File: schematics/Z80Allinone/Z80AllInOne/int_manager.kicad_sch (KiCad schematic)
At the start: 8 parts, among them U25 74LS32, U26 74LS148, U28 74LS373

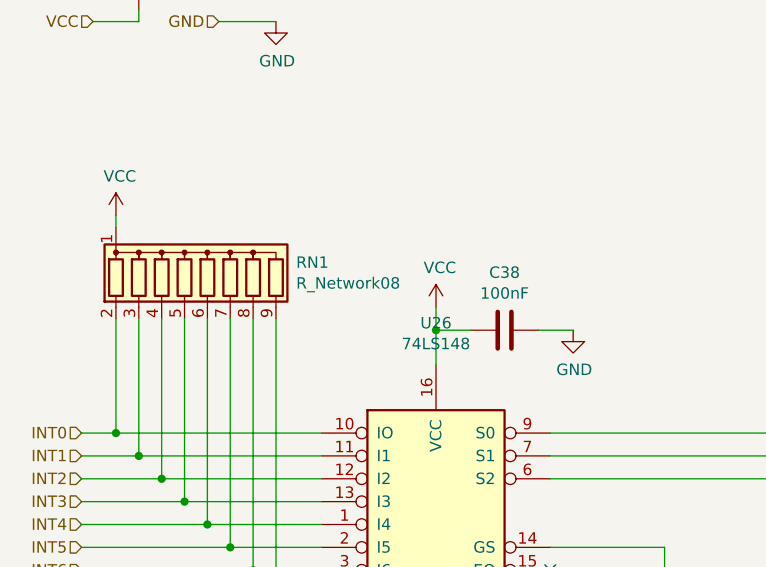
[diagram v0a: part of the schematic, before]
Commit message: Latest changes for adapt source to support Z80AllInOne adding some macros and latest schematic improvements
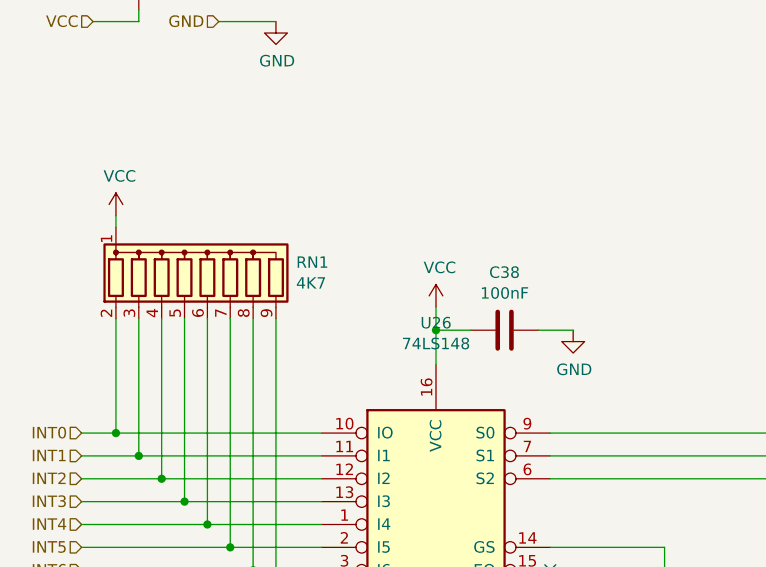
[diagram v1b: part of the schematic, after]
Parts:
- RN1: value R_Network08 -> 4K7
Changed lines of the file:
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@@
       (effects (font (size 1.27 1.27)) (justify left))
     )
-    (property "Value" "R_Network08" (id 1) (at 96.2152 59.563 0)
+    (property "Value" "4K7" (id 1) (at 96.2152 59.563 0)
       (effects (font (size 1.27 1.27)) (justify left))
     )

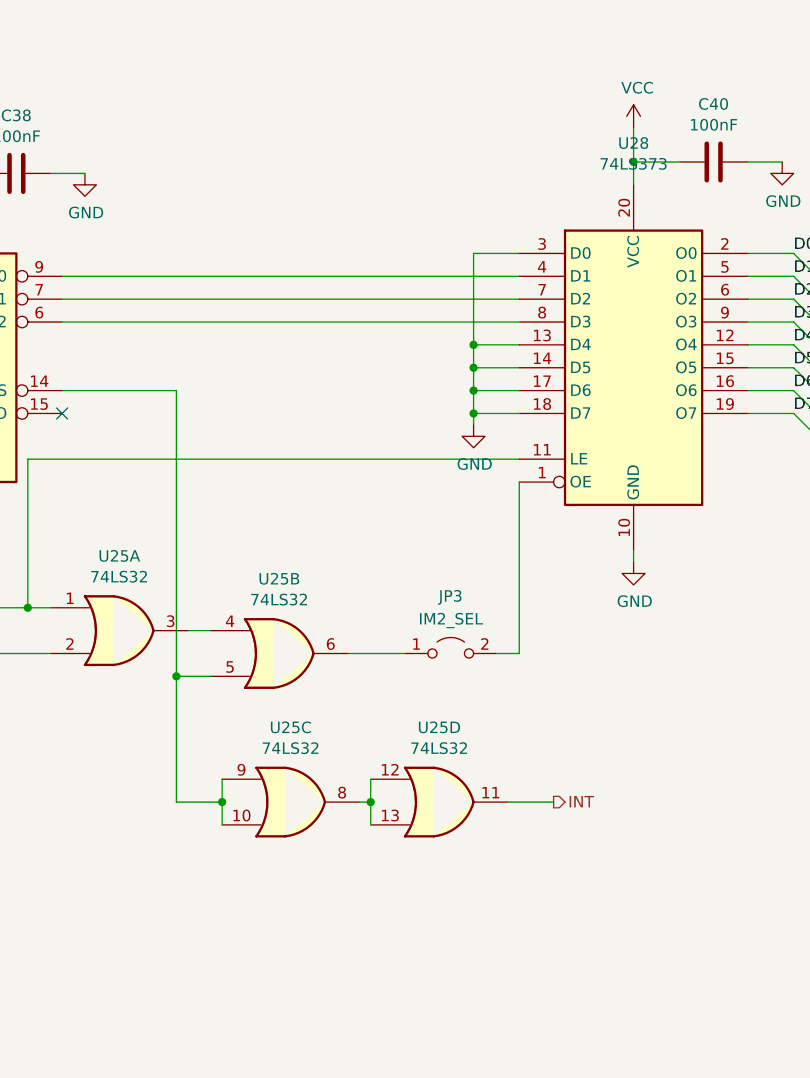
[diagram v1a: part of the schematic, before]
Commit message: Added IM 2 based routines software support
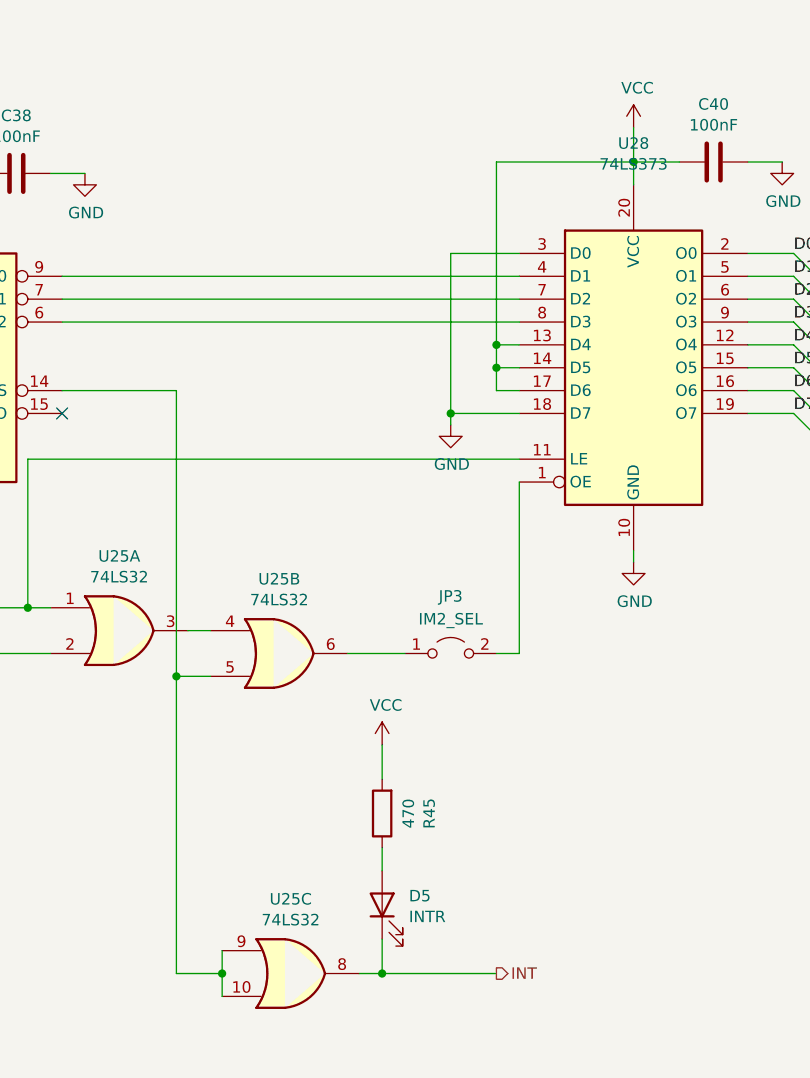
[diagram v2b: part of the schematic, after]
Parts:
- removed unit 4 of U25
- added D5: INTR, LED_THT:LED_D3.0mm, symbol Device:LED
- added R45: 470, Resistor_THT:R_Axial_DIN0207_L6.3mm_D2.5mm_P10.16mm_Horizontal, symbol Device:R
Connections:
- net GND: no longer U28.13 (D4), U28.14 (D5), U28.17 (D6)
- net INT: now also U25.8, D5.1 (K)
- net VCC: now also U28.13 (D4), U28.14 (D5), U28.17 (D6), R45.2
- new net: D5.2 (A), R45.1
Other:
- moved on the sheet: U25C

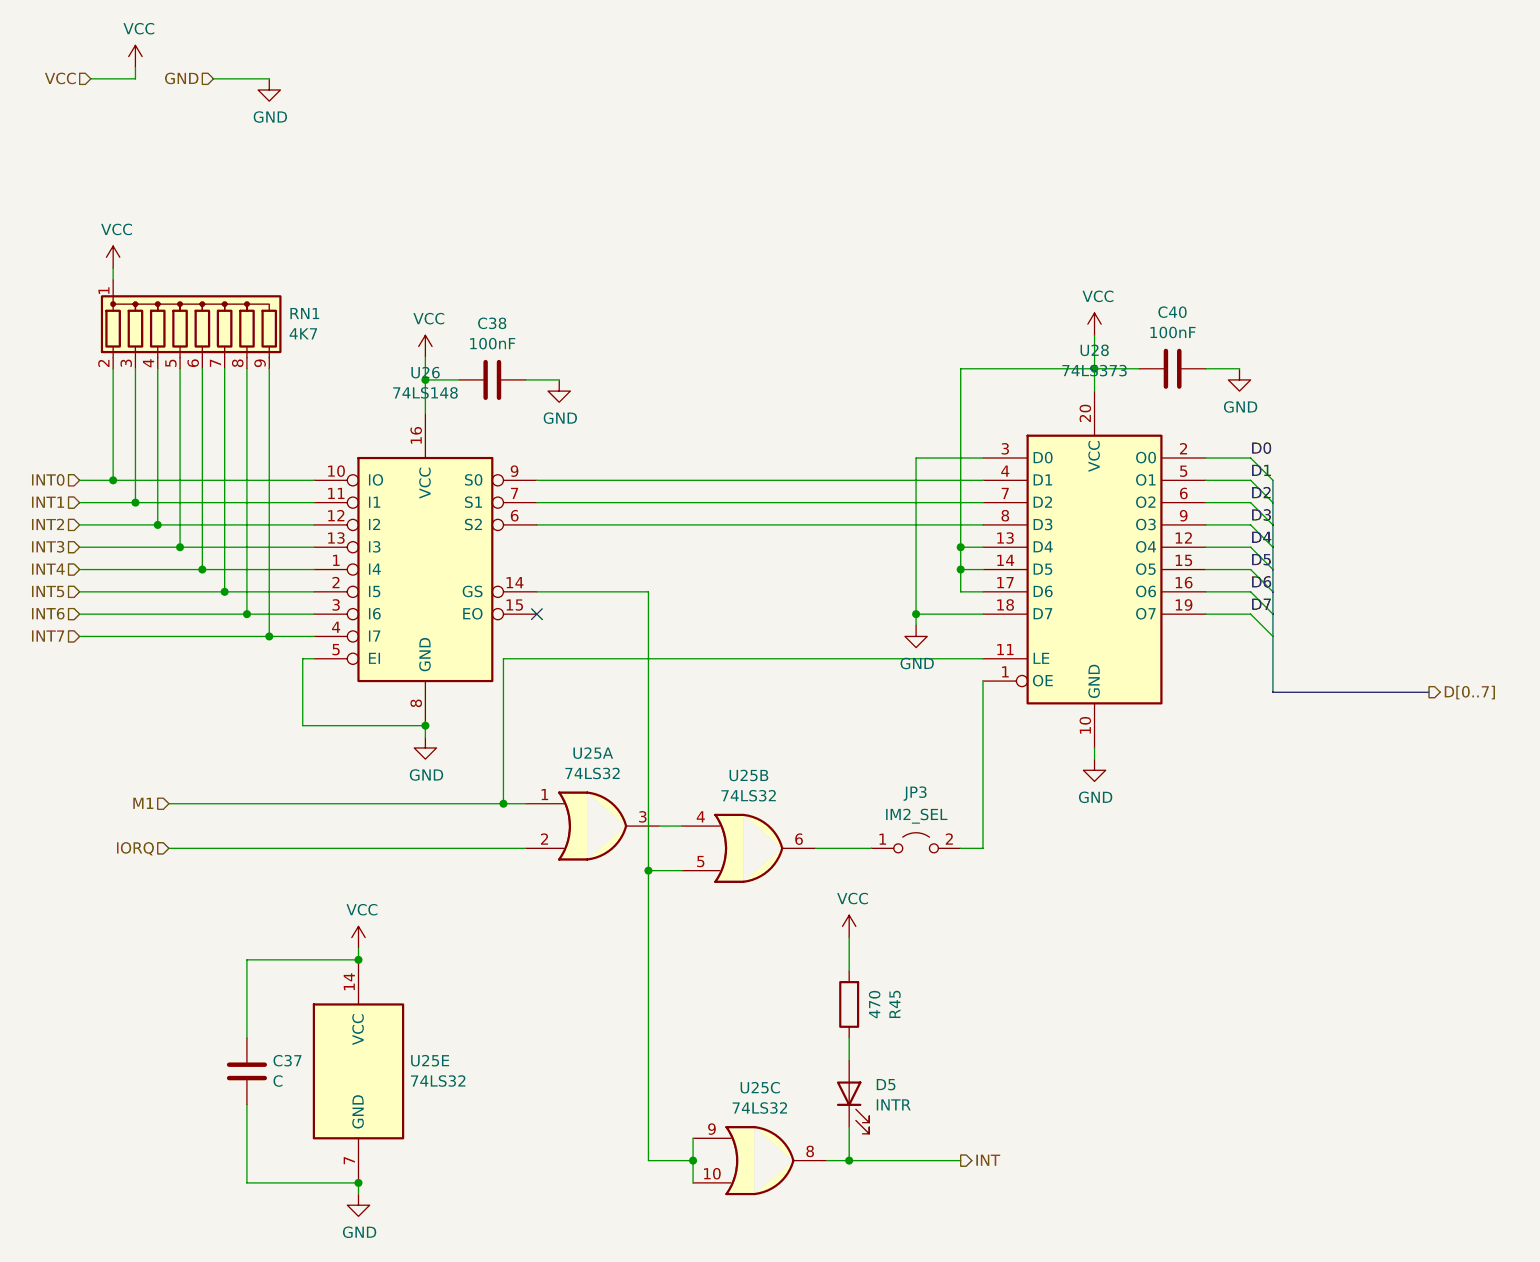
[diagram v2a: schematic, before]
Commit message: Latest changes and replace CTC for 8253 PIT
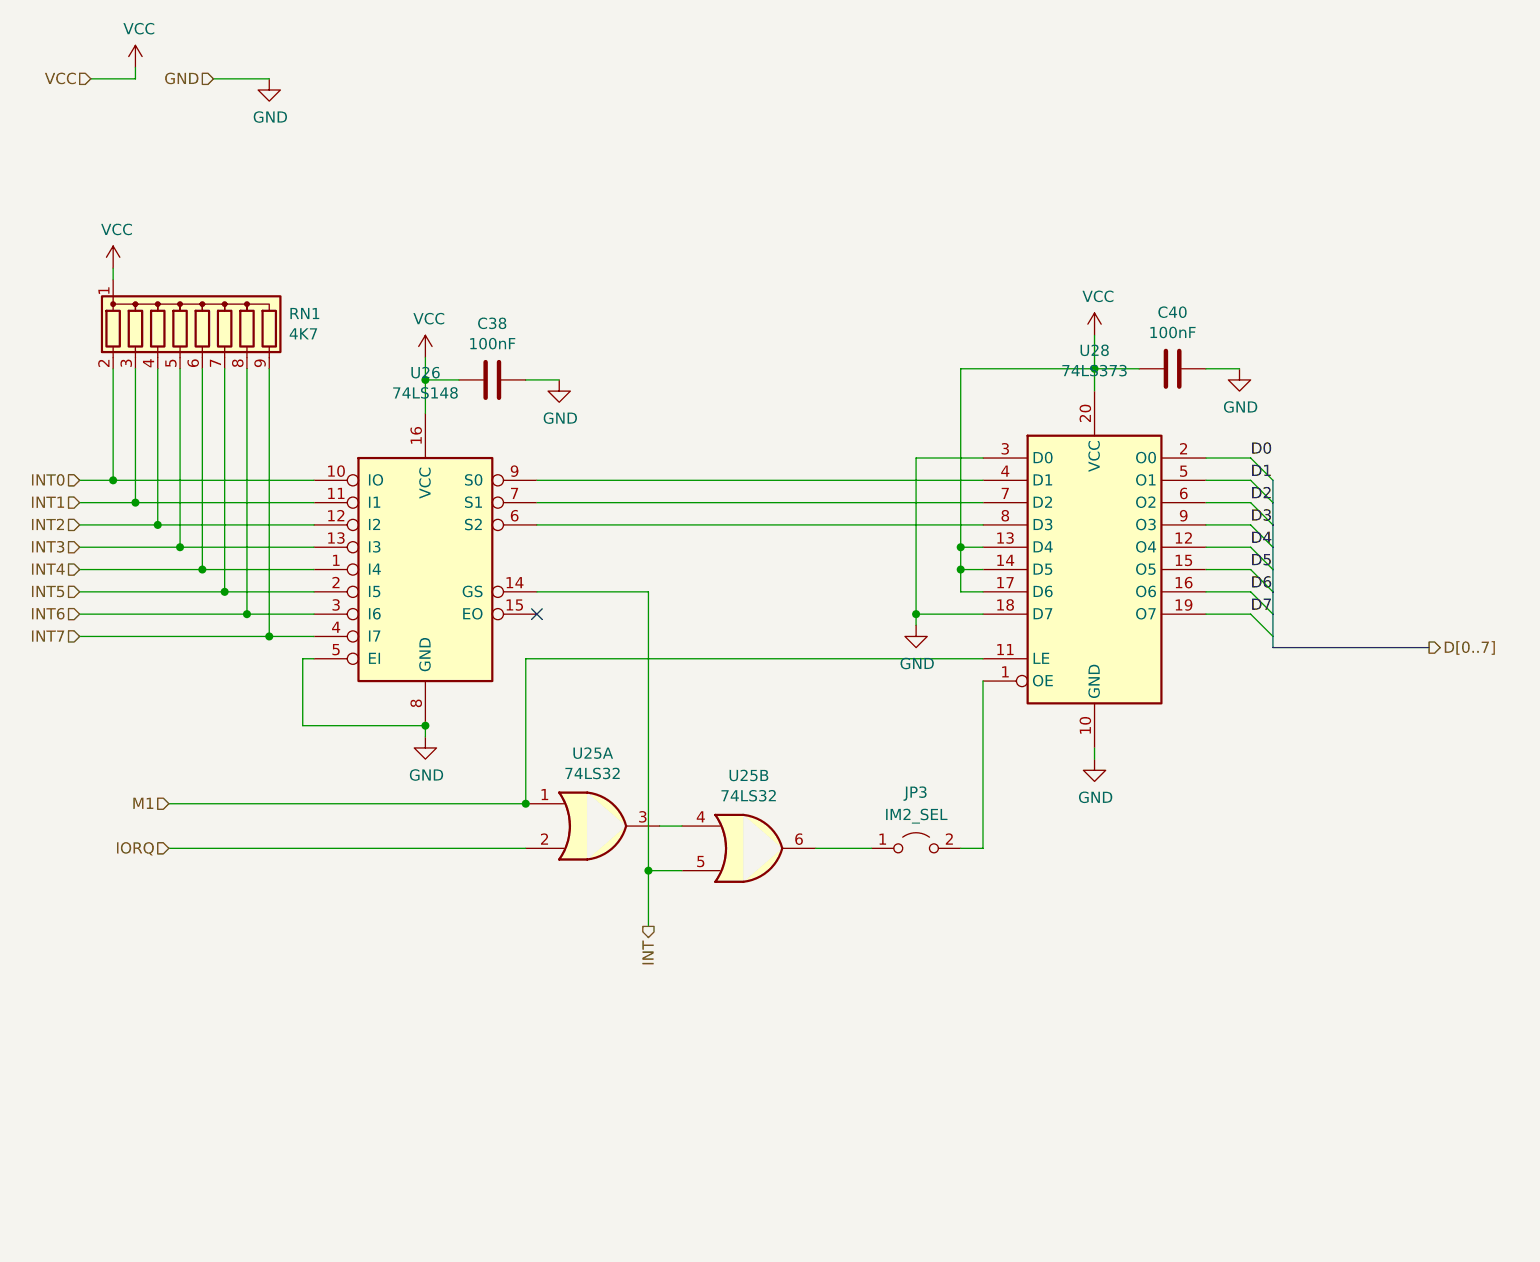
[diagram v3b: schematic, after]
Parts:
- removed C37: C, Capacitor_THT:C_Disc_D7.0mm_W2.5mm_P5.00mm, symbol Device:C
- removed D5: INTR, LED_THT:LED_D3.0mm, symbol Device:LED
- removed R45: 470, Resistor_THT:R_Axial_DIN0207_L6.3mm_D2.5mm_P10.16mm_Horizontal, symbol Device:R
- removed unit 5 of U25
- removed unit 3 of U25
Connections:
- net INT: now also U25.5, U26.14 (GS)
